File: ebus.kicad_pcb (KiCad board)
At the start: 2 copper layers, 99.6 x 56.9 mm, 45 parts, among them J1 EBUS, J2 UART, J3 USB_B_Micro, J4 PWR, J5 SERVICE, J6 PROG, Q1 BC337, U1 LM393, U2 4N25, U3 L7805, U4 4N25, U5 ESP-12F, U6 AMS1117-3.3

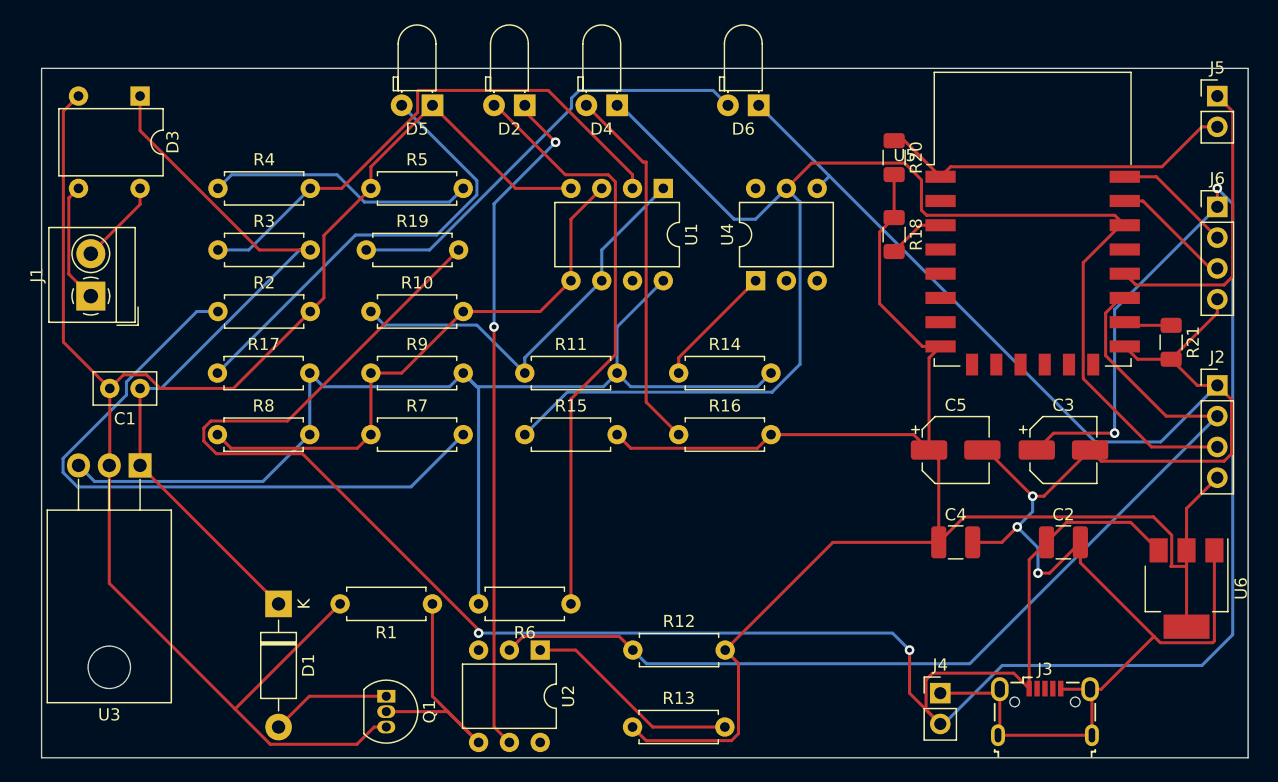
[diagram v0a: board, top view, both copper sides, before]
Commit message: PCB redesigned and with labels
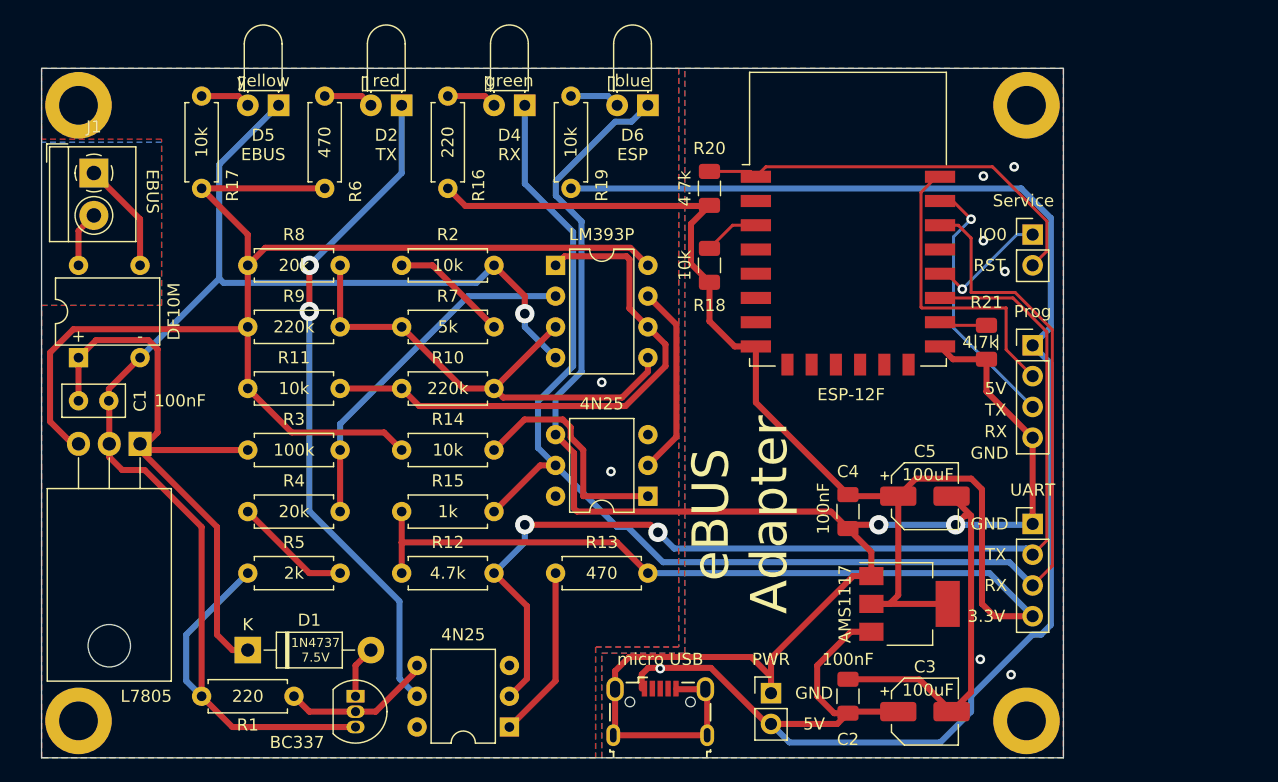
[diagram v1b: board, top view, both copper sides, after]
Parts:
- removed J4: PWR, Connector_PinHeader_2.54mm:PinHeader_1x02_P2.54mm_Vertical
- removed Q1: BC337, Package_TO_SOT_THT:TO-92_Inline
- removed U3: L7805, Package_TO_SOT_THT:TO-220-3_Horizontal_TabDown
- added BC337: BC337, Package_TO_SOT_THT:TO-92_Inline, F.Cu at (66.0, 134.6)
- added L7805: L7805, Package_TO_SOT_THT:TO-220-3_Horizontal_TabDown, F.Cu at (48.3, 113.8)
- added PWR: PWR, Connector_PinHeader_2.54mm:PinHeader_1x02_P2.54mm_Vertical, F.Cu at (100.3, 134.4)
- added REF**: MountingHole_3.2mm_M3_ISO14580_Pad, MountingHole:MountingHole_3.2mm_M3_ISO14580_Pad, F.Cu at (121.4, 136.7)
- added REF**: MountingHole_3.2mm_M3_ISO14580_Pad, MountingHole:MountingHole_3.2mm_M3_ISO14580_Pad, F.Cu at (121.4, 85.9)
- added REF**: MountingHole_3.2mm_M3_ISO14580_Pad, MountingHole:MountingHole_3.2mm_M3_ISO14580_Pad, F.Cu at (43.2, 85.9)
- added REF**: MountingHole_3.2mm_M3_ISO14580_Pad, MountingHole:MountingHole_3.2mm_M3_ISO14580_Pad, F.Cu at (43.2, 136.7)
- C2, C4: footprint Capacitor_SMD:C_1210_3225Metric -> Capacitor_SMD:C_1206_3216Metric
- micro USB: renamed from J3
- moved R6 46.6 mm to (63.5, 85.1), turned to 270 degrees
- moved R16 33.8 mm to (73.7, 85.1), turned to 270 degrees
- moved R5 33.3 mm to (57.1, 124.5)
- moved micro USB 31.8 mm to (91.2, 135.9)
- moved R4 26.8 mm to (57.1, 119.4)
- moved C3 24.4 mm to (113.0, 135.9)
- moved R17 22.9 mm to (53.3, 85.1), turned to 270 degrees
- moved AMS1117 22.9 mm to (111.8, 127.0), turned to 0 degrees
- moved DF10M 22.2 mm to (43.2, 106.7), turned to 90 degrees
- moved C2 21.8 mm to (106.7, 134.6), turned to 90 degrees
- moved R19 21.1 mm to (83.8, 85.1), turned to 270 degrees
- moved 4N25 19.9 mm to (90.2, 118.1), turned to 180 degrees
- moved R3 19.3 mm to (64.8, 114.3), turned to 180 degrees
- moved Prog 19.1 mm to (121.9, 105.7)
- moved UART 19.1 mm to (121.9, 120.4)
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- renumbered U4 to 4N25, U2 to 4N25, U6 to AMS1117, D3 to DF10M, U5 to ESP-12F, U1 to LM393P, J6 to Prog, J5 to Service, J2 to UART
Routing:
- net +5VP: track 233.1 -> 140.1 mm, vias 4 -> 1
- net Net-(R2-Pad1): track 54.9 -> 9.72 mm
- net Net-(D2-Pad2): track 49.0 -> 4.13 mm
- net Net-(D5-Pad2): track 37.5 -> 4.13 mm
- net Net-(D6-Pad2): track 36.3 -> 4.13 mm
- net Net-(D4-Pad2): track 30.5 -> 4.13 mm
- net GNDD: track 139.1 -> 118.0 mm, vias 0 -> 3
- net +3V3: track 139.1 -> 155.9 mm
- net Net-(U1-Pad7): track 0.00 -> 15.9 mm
- net P_TX: track 9.72 -> 25.2 mm
- net Net-(R3-Pad1): track 44.7 -> 29.4 mm
- net GPIO0: track 25.0 -> 10.0 mm, vias 0 -> 1
- net GNDREF: track 168.1 -> 182.2 mm, vias 3 -> 8
- net SIGNAL: track 62.3 -> 49.7 mm
- net Net-(R4-Pad1): track 22.1 -> 9.72 mm
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- added copper zone on B.Cu, net GNDD
- added copper zone on F.Cu, net GNDD
- added copper zone on B.Cu, net GNDREF
- added copper zone on F.Cu, net GNDREF
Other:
- board size 99.6 x 56.9 mm -> 84.3 x 56.9 mm
- net class Power added: clearance 0.4, trace_width 0.5, via_dia 1.6, via_drill 0.8
- rule trace_min: 0.2 -> 0
- board text added: "+"
- board text added: "-"
- board text added: "100k"
- board text added: "100nF"
- board text added: "100uF"
- board text added: "10k"
- board text added: "1N4737 7.5V"
- board text added: "1k"
- board text added: "20k"
- board text added: "220"
- board text added: "220k"
- board text added: "2k"
- board text added: "3.3V"
- board text added: "4.7k"
- board text added: "470"
- board text added: "5V"
- board text added: "5k"
- board text added: "EBUS"
- board text added: "ESP"
- board text added: "GND"
- board text added: "IO0"
- board text added: "RST"
- board text added: "RX"
- board text added: "TX"
- board text added: "blue"
- board text added: "eBUS Adapter"
- board text added: "green"
- board text added: "red"
- board text added: "yellow"
- board text added: "~"
